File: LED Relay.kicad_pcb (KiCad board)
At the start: 2 copper layers, 38.1 x 19.1 mm, 43 parts, among them J1 TEST_1P, J2 TEST_1P, J3 TEST_1P, J4 TEST_1P, J5 TEST_1P, J6 TEST_1P, J7 TEST_1P, J8 TEST_1P, J9 Header, U1 LT3014IDD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

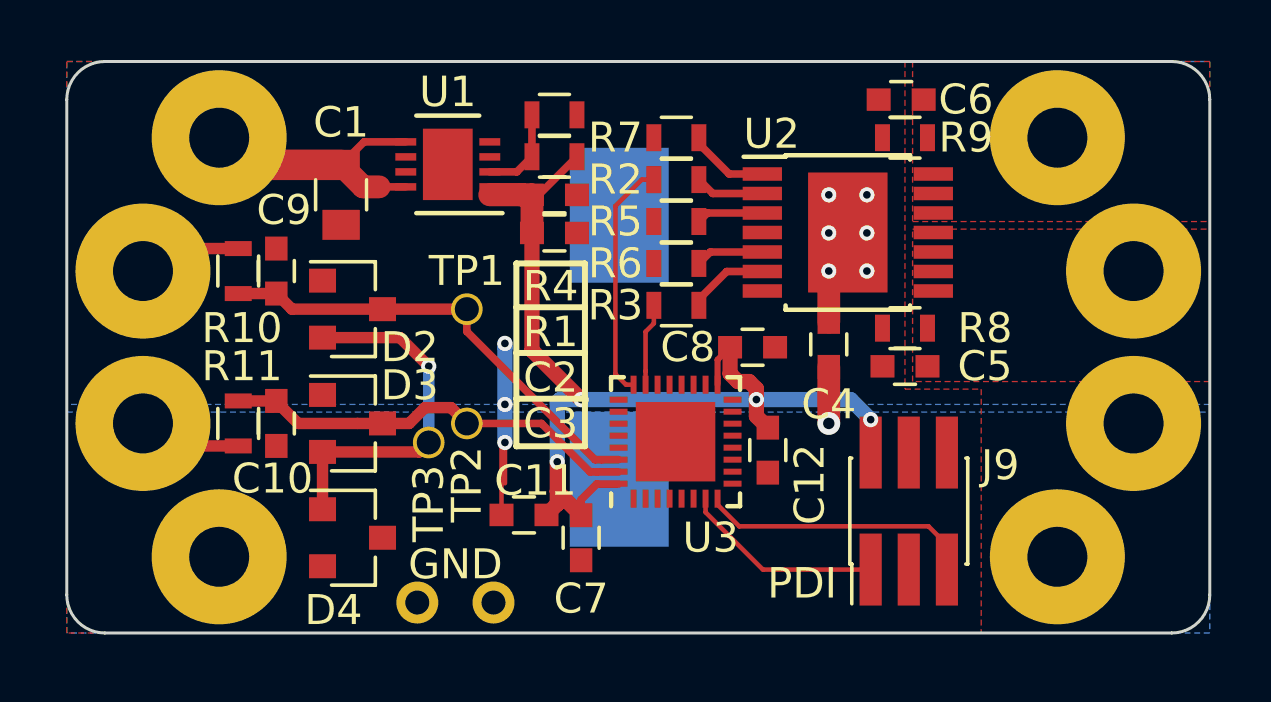
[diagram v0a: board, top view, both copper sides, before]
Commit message: Upped Rev to 2.1. Added R12 and R13. Moved connections on micro-controller.
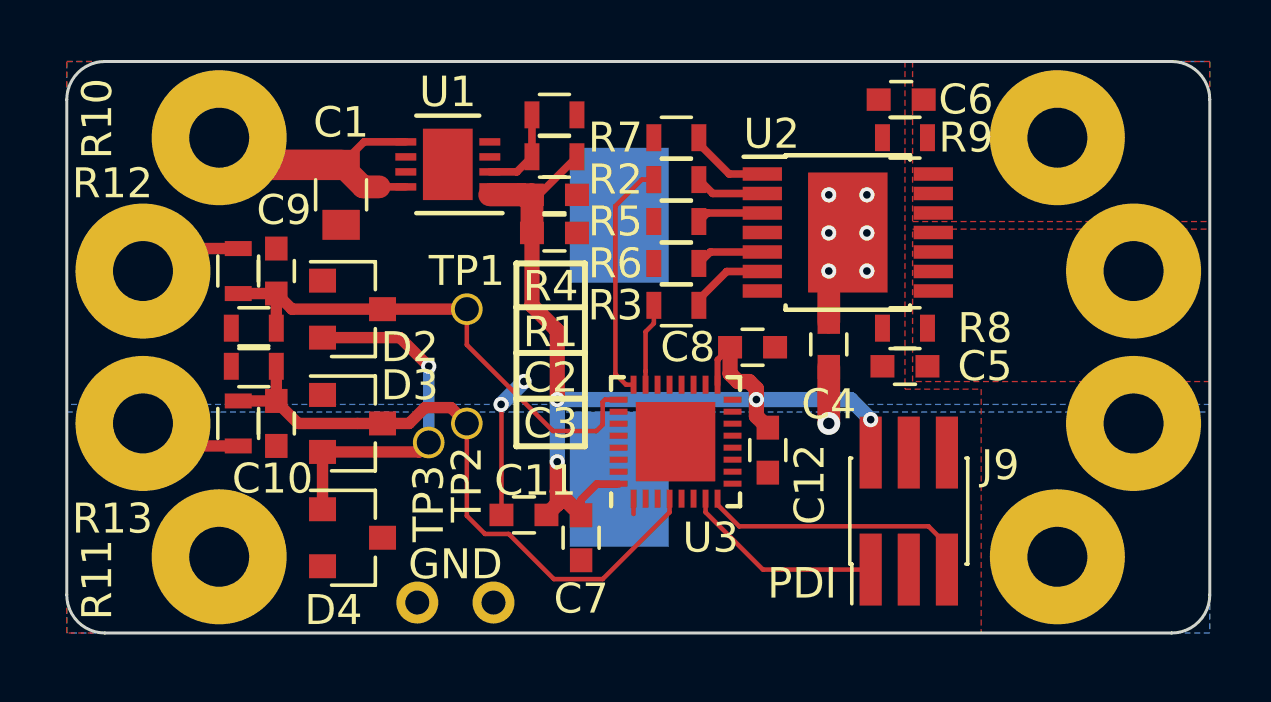
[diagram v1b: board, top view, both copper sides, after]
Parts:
- added R12: 47k, Resistors_SMD:R_0603, F.Cu at (41.8, 36.8)
- added R13: 47k, Resistors_SMD:R_0603, F.Cu at (41.8, 38.1)
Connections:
- C9 pad 1: Net-(C9-Pad1) -> ACC1_IN
- D2 pad 3: Net-(C9-Pad1) -> ACC1_IN
- R10 pad 1: Net-(C9-Pad1) -> ACC1_IN
- TP1 pad 1: Net-(C9-Pad1) -> ACC1_IN
- U3 pad 25: Net-(U3-Pad25) -> ACC1_IN
- U3 pad 30: Net-(C9-Pad1) -> Net-(U3-Pad30)
- U3 pad 31: Net-(C10-Pad1) -> Net-(U3-Pad31)
- U3 pad 4: Net-(U3-Pad4) -> Net-(C10-Pad1)
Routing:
- net ACC1_IN: track 0.00 -> 17.3 mm
- net Net-(C9-Pad1): track 15.4 -> 0.00 mm
- net Net-(C10-Pad1): track 14.1 -> 21.6 mm
- net GNDD: track 7.15 -> 5.30 mm, vias 3 -> 2
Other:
- board text added: "Rev 2.1"
- board text removed: "Rev 2.0"

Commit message: Upped Rev to 2.2. Added ACC1 connect to PD2 on micro-controller.
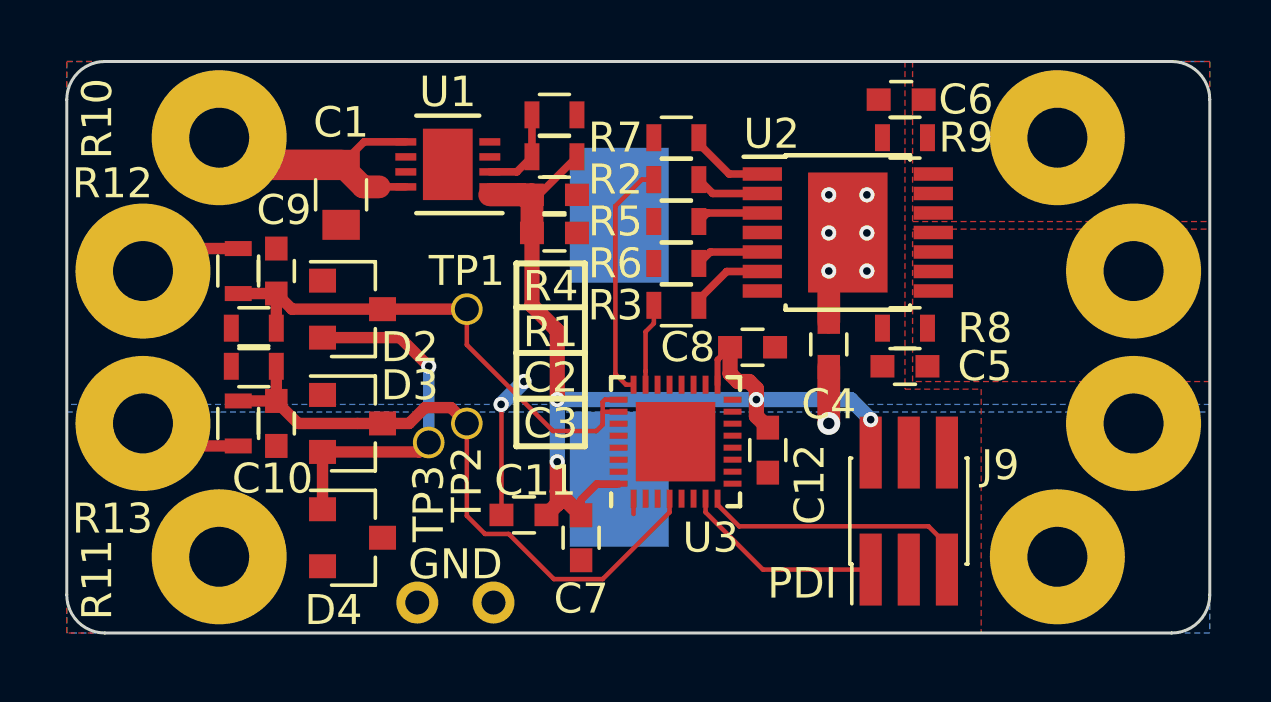
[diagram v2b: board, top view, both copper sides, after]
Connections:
- U3 pad 26: Net-(U3-Pad26) -> ACC1_IN
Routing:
- net ACC1_IN: track 17.3 -> 17.8 mm
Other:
- board text added: "Rev 2.2"
- board text removed: "Rev 2.1"
